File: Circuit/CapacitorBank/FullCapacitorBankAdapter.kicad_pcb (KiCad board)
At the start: 2 copper layers, 114.3 x 61 mm, 45 parts, among them J1 AC Power In, J2 Output+, J3 Output-, J4 To Control, T1 6:6:75+75, U1 L7812, U2 LM393, U3 LM393, U4 PC817

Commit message: [Circuit] Add a bypass diode to capacitor bank adapter for safety
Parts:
- added D7: 1N4007, Diode_THT:D_DO-41_SOD81_P10.16mm_Horizontal, F.Cu at (142.2, 64.8)
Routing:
- net /PowerOut-: track 107.3 -> 113.7 mm
- net /PowerOut+: track 96.8 -> 103.1 mm
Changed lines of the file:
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@@
     (thickness 1.6)
     (drawings 17)
-    (tracks 147)
+    (tracks 150)
     (zones 0)
-    (modules 45)
+    (modules 46)
     (nets 40)
   )
@@
     (add_net "Net-(R6-Pad2)")
     (add_net "Net-(R8-Pad2)")
+  )
+  (module Diode_THT:D_DO-41_SOD81_P10.16mm_Horizontal (layer F.Cu)
+    (at 142.24 64.77 270)
+    (descr "Diode, DO-41_SOD81 series, Axial, Horizontal, pin pitch=10.16mm, , length*diameter=5.2*2.7mm^2, , http://www.diodes.com/_files/packages/DO-41%20(Plastic).pdf")
+    (tags "Diode DO-41_SOD81 series Axial Horizontal pin pitch 10.16mm  length 5.2mm diameter 2.7mm")
+    (fp_text reference D7 (at 5.08 -2.47 90) (layer F.SilkS)
+      (effects (font (size 1 1) (thickness 0.15)))
+    )
+    (fp_text value 1N4007 (at 5.08 2.47 90) (layer F.Fab)
+      (effects (font (size 1 1) (thickness 0.15)))
+    )
+    (fp_text user K (at 0 -2.1 90) (layer F.SilkS)
+      (effects (font (size 1 1) (thickness 0.15)))
+    )
+    (fp_text user K (at 0 -2.1 90) (layer F.Fab)
+      (effects (font (size 1 1) (thickness 0.15)))
+    )
+    (fp_text user %R (at 5.47 0 90) (layer F.Fab)
+      (effects (font (size 1 1) (thickness 0.15)))
+    )
+    (fp_line (start 11.51 -1.6) (end -1.35 -1.6) (layer F.CrtYd) (width 0.05))
+    (fp_line (start 11.51 1.6) (end 11.51 -1.6) (layer F.CrtYd) (width 0.05))
+    (fp_line (start -1.35 1.6) (end 11.51 1.6) (layer F.CrtYd) (width 0.05))
+    (fp_line (start -1.35 -1.6) (end -1.35 1.6) (layer F.CrtYd) (width 0.05))
+    (fp_line (start 3.14 -1.47) (end 3.14 1.47) (layer F.SilkS) (width 0.12))
+    (fp_line (start 3.38 -1.47) (end 3.38 1.47) (layer F.SilkS) (width 0.12))
+    (fp_line (start 3.26 -1.47) (end 3.26 1.47) (layer F.SilkS) (width 0.12))
+    (fp_line (start 8.82 0) (end 7.8 0) (layer F.SilkS) (width 0.12))
+    (fp_line (start 1.34 0) (end 2.36 0) (layer F.SilkS) (width 0.12))
+    (fp_line (start 7.8 -1.47) (end 2.36 -1.47) (layer F.SilkS) (width 0.12))
+    (fp_line (start 7.8 1.47) (end 7.8 -1.47) (layer F.SilkS) (width 0.12))
+    (fp_line (start 2.36 1.47) (end 7.8 1.47) (layer F.SilkS) (width 0.12))
+    (fp_line (start 2.36 -1.47) (end 2.36 1.47) (layer F.SilkS) (width 0.12))
+    (fp_line (start 3.16 -1.35) (end 3.16 1.35) (layer F.Fab) (width 0.1))
+    (fp_line (start 3.36 -1.35) (end 3.36 1.35) (layer F.Fab) (width 0.1))
+    (fp_line (start 3.26 -1.35) (end 3.26 1.35) (layer F.Fab) (width 0.1))
+    (fp_line (start 10.16 0) (end 7.68 0) (layer F.Fab) (width 0.1))
+    (fp_line (start 0 0) (end 2.48 0) (layer F.Fab) (width 0.1))
+    (fp_line (start 7.68 -1.35) (end 2.48 -1.35) (layer F.Fab) (width 0.1))
+    (fp_line (start 7.68 1.35) (end 7.68 -1.35) (layer F.Fab) (width 0.1))
+    (fp_line (start 2.48 1.35) (end 7.68 1.35) (layer F.Fab) (width 0.1))
+    (fp_line (start 2.48 -1.35) (end 2.48 1.35) (layer F.Fab) (width 0.1))
+    (pad 2 thru_hole oval (at 10.16 0 270) (size 2.2 2.2) (drill 1.1) (layers *.Cu *.Mask)
+      (net 2 /PowerOut-))
+    (pad 1 thru_hole rect (at 0 0 270) (size 2.2 2.2) (drill 1.1) (layers *.Cu *.Mask)
+      (net 1 /PowerOut+))
+    (model ${KISYS3DMOD}/Diode_THT.3dshapes/D_DO-41_SOD81_P10.16mm_Horizontal.wrl
+      (at (xyz 0 0 0))
+      (scale (xyz 1 1 1))
+      (rotate (xyz 0 0 0))
+    )
   )
   (module Capacitor_THT:CP_Radial_D4.0mm_P2.00mm (layer F.Cu)
@@
   (gr_line (start 105.41 74.93) (end 115.57 74.93) (layer F.Mask) (width 0.15))
   (gr_circle (center 142.24 35.56) (end 143.51 35.56) (layer Edge.Cuts) (width 0.05))
-  (gr_text "M. Gong" (at 144.78 68.58) (layer F.SilkS)
+  (gr_text "M. Gong" (at 149.86 68.58) (layer F.SilkS)
     (effects (font (size 1 1) (thickness 0.15)))
   )
@@
   (segment (start 114.3 58.42) (end 106.68 58.42) (width 0.25) (layer B.Cu) (net 1))
   (segment (start 119.38 63.5) (end 124.46 58.42) (width 0.25) (layer B.Cu) (net 1) (status 10))
-  (segment (start 124.46 58.42) (end 148.59 58.42) (width 0.25) (layer B.Cu) (net 1))
+  (segment (start 142.24 64.77) (end 142.24 58.42) (width 0.25) (layer B.Cu) (net 1))
+  (segment (start 124.46 58.42) (end 142.24 58.42) (width 0.25) (layer B.Cu) (net 1))
+  (segment (start 142.24 58.42) (end 148.59 58.42) (width 0.25) (layer B.Cu) (net 1))
   (segment (start 88.98 76.12) (end 88.82 76.12) (width 0.25) (layer B.Cu) (net 2) (status 30))
   (segment (start 88.98 76.12) (end 88.98 81.28) (width 0.25) (layer B.Cu) (net 2) (status 30))
@@
   (segment (start 91.44 83.82) (end 88.98 81.36) (width 0.25) (layer B.Cu) (net 2) (status 20))
   (segment (start 88.9 81.28) (end 86.36 83.82) (width 0.25) (layer B.Cu) (net 2) (status 10))
+  (segment (start 142.24 74.93) (end 142.24 81.28) (width 0.25) (layer B.Cu) (net 2))
   (segment (start 114.3 71.12) (end 114.3 73.66) (width 0.25) (layer B.Cu) (net 3) (status 30))
   (segment (start 114.3 78.74) (end 114.3 76.2) (width 0.25) (layer B.Cu) (net 4) (status 30))

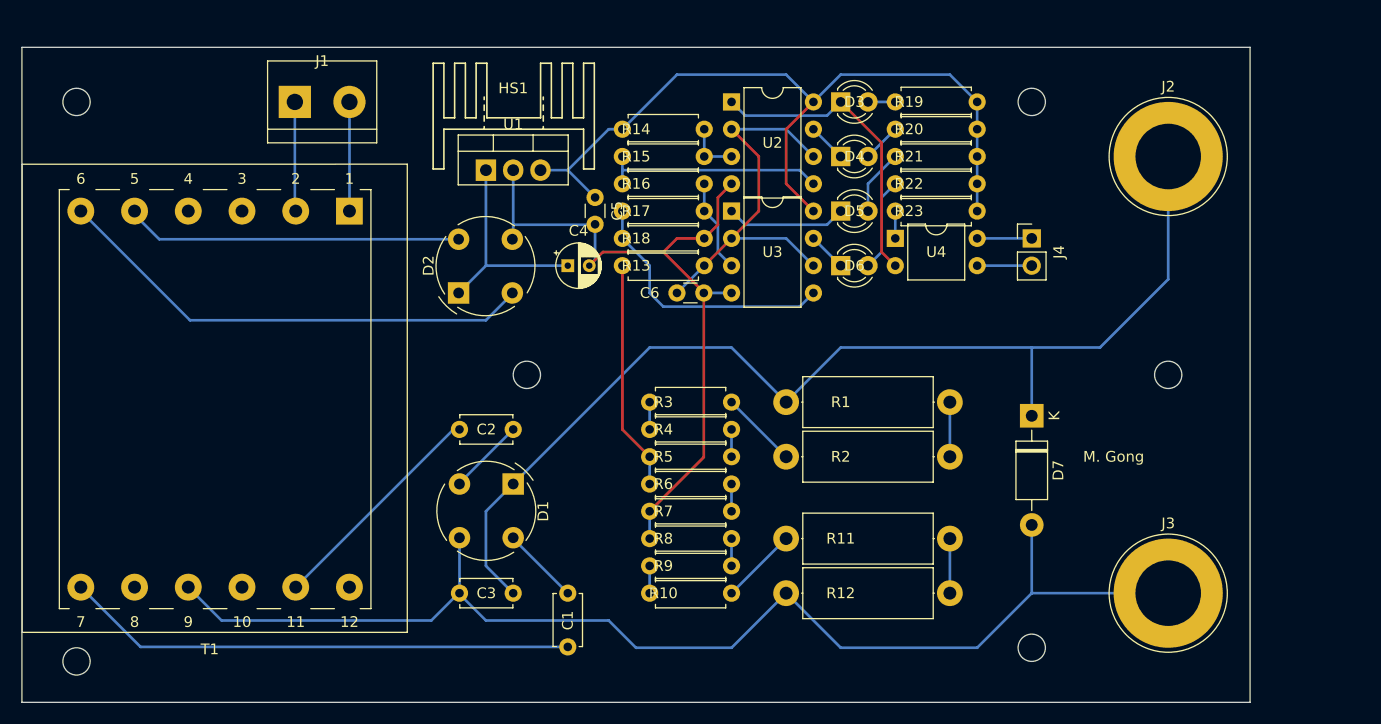
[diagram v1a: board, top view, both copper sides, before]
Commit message: [Circuit] Change the decoupling capacitors to a larger ones
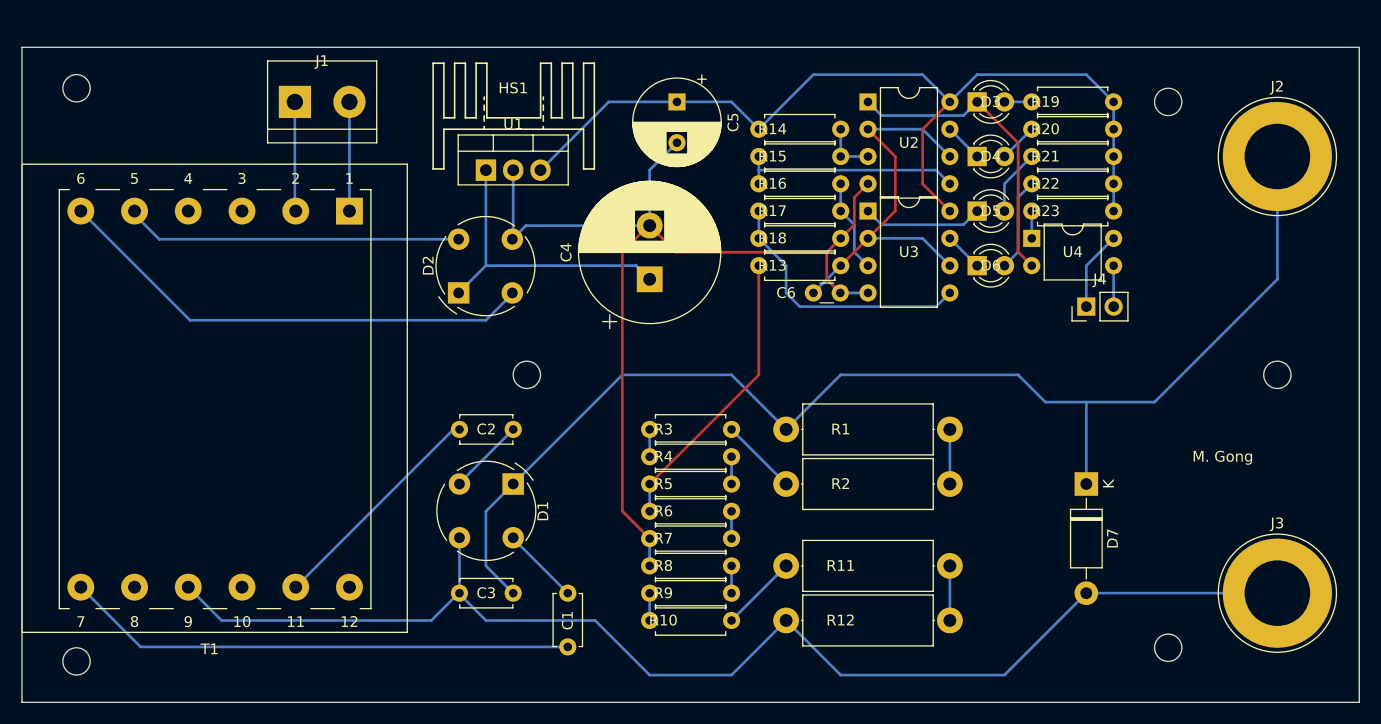
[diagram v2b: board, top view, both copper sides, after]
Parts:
- C4: value 1uF -> 2200uF; footprint Capacitor_THT:CP_Radial_D4.0mm_P2.00mm -> Capacitor_THT:CP_Radial_D13.0mm_P5.00mm
- C5: footprint Capacitor_THT:C_Disc_D3.0mm_W1.6mm_P2.50mm -> Capacitor_THT:CP_Radial_D8.0mm_P3.80mm
- moved R19 12.7 mm to (149.9, 35.6)
- moved R20 12.7 mm to (149.9, 38.1)
- moved R21 12.7 mm to (149.9, 40.6)
- moved R22 12.7 mm to (149.9, 43.2)
- moved R23 12.7 mm to (142.2, 45.7)
- moved U4 12.7 mm to (142.2, 48.3)
- moved C6 12.7 mm to (121.9, 53.3)
- moved D3 12.7 mm to (137.2, 35.6)
- moved D4 12.7 mm to (137.2, 40.6)
- moved D5 12.7 mm to (137.2, 45.7)
- moved D6 12.7 mm to (137.2, 50.8)
- moved R15 12.7 mm to (116.8, 40.6)
- moved R17 12.7 mm to (116.8, 45.7)
- moved U2 12.7 mm to (127.0, 35.6)
- moved U3 12.7 mm to (127.0, 45.7)
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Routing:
- net GND: track 69.1 -> 94.9 mm
- net /PowerOut+: track 103.1 -> 116.6 mm
- net +12V: track 73.5 -> 84.7 mm
- net Net-(C4-Pad1): track 20.1 -> 28.2 mm
- net /PowerOut-: track 113.7 -> 119.6 mm
- net Net-(R13-Pad2): track 21.4 -> 27.1 mm
- net /ControlSignal: track 5.08 -> 7.40 mm
- net /ControlGND: track 5.08 -> 3.81 mm
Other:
- board size 114.3 x 61 mm -> 124.5 x 61 mm

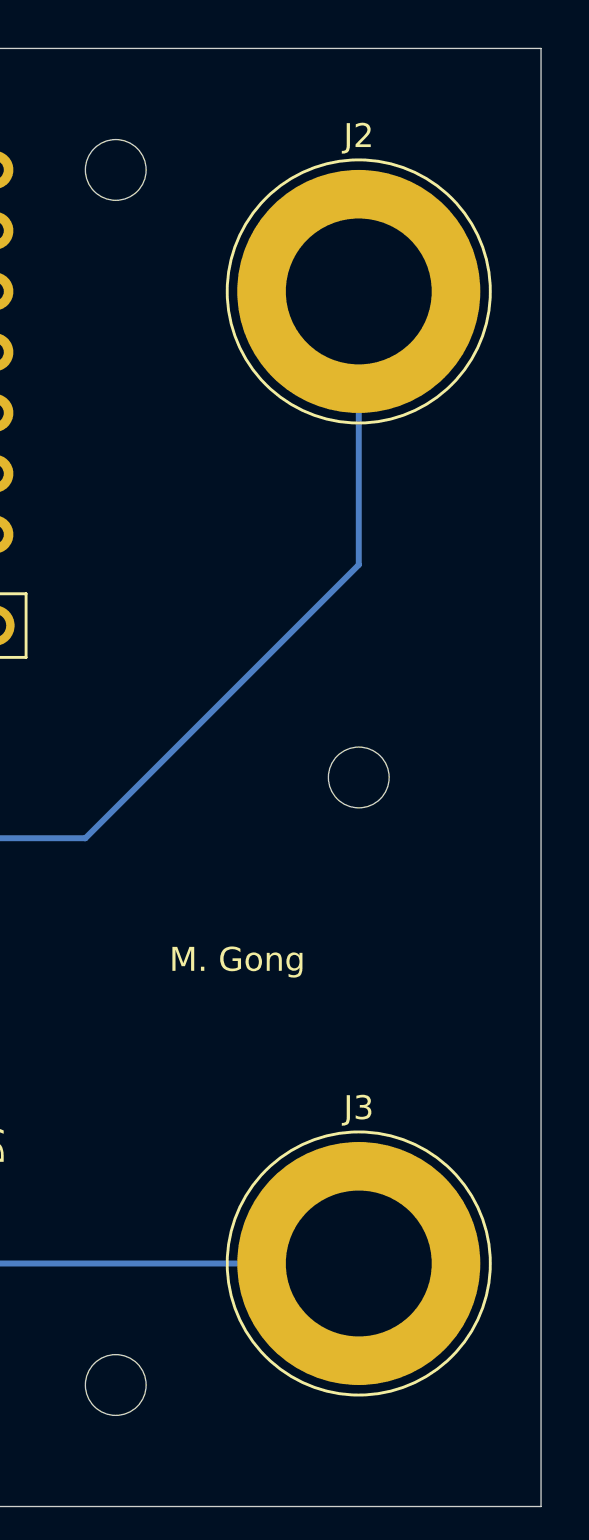
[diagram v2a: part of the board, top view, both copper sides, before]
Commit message: [Circuit] Use M6 bolt as the connectors of capacitor bank and starter
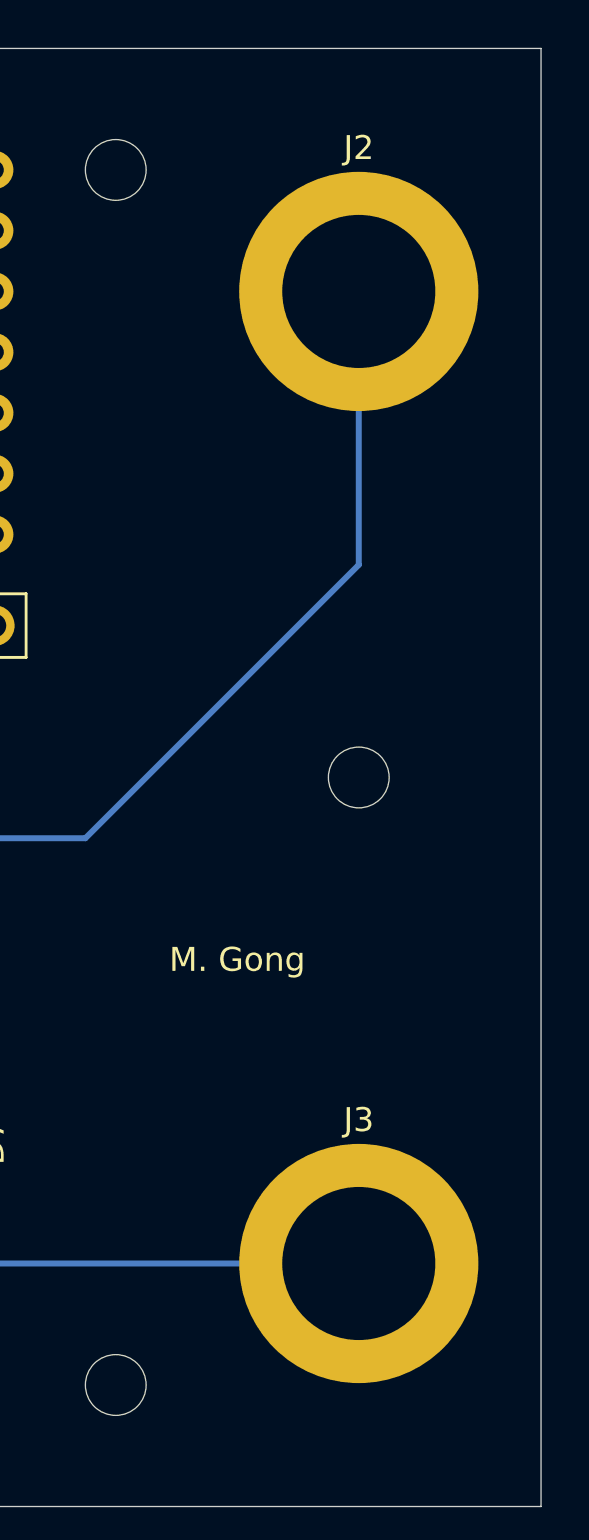
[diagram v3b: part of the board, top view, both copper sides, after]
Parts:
- J2, J3: footprint Connector:Banana_Jack_1Pin -> MountingHole:MountingHole_6.4mm_M6_ISO14580_Pad
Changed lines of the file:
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@@
     (add_net "Net-(R8-Pad2)")
+  )
+  (module MountingHole:MountingHole_6.4mm_M6_ISO14580_Pad (layer F.Cu)
+    (at 165.1 40.64)
+    (descr "Mounting Hole 6.4mm, M6, ISO14580")
+    (tags "mounting hole 6.4mm m6 iso14580")
+    (attr virtual)
+    (fp_text reference J2 (at 0 -6) (layer F.SilkS)
+      (effects (font (size 1 1) (thickness 0.15)))
+    )
+    (fp_text value Output+ (at 0 6) (layer F.Fab)
+      (effects (font (size 1 1) (thickness 0.15)))
+    )
+    (fp_circle (center 0 0) (end 5.25 0) (layer F.CrtYd) (width 0.05))
+    (fp_circle (center 0 0) (end 5 0) (layer Cmts.User) (width 0.15))
+    (fp_text user %R (at 0.3 0) (layer F.Fab)
+      (effects (font (size 1 1) (thickness 0.15)))
+    )
+    (pad 1 thru_hole circle (at 0 0) (size 10 10) (drill 6.4) (layers *.Cu *.Mask)
+      (net 1 /PowerOut+))
+  )
+  (module MountingHole:MountingHole_6.4mm_M6_ISO14580_Pad (layer F.Cu)
+    (at 165.1 81.28)
+    (descr "Mounting Hole 6.4mm, M6, ISO14580")
+    (tags "mounting hole 6.4mm m6 iso14580")
+    (attr virtual)
+    (fp_text reference J3 (at 0 -6) (layer F.SilkS)
+      (effects (font (size 1 1) (thickness 0.15)))
+    )
+    (fp_text value Output- (at 0 6) (layer F.Fab)
+      (effects (font (size 1 1) (thickness 0.15)))
+    )
+    (fp_circle (center 0 0) (end 5.25 0) (layer F.CrtYd) (width 0.05))
+    (fp_circle (center 0 0) (end 5 0) (layer Cmts.User) (width 0.15))
+    (fp_text user %R (at 0.3 0) (layer F.Fab)
+      (effects (font (size 1 1) (thickness 0.15)))
+    )
+    (pad 1 thru_hole circle (at 0 0) (size 10 10) (drill 6.4) (layers *.Cu *.Mask)
+      (net 2 /PowerOut-))
   )
   (module Capacitor_THT:CP_Radial_D13.0mm_P5.00mm (layer F.Cu)
@@
     )
   )
-  (module Connector:Banana_Jack_1Pin (layer F.Cu)
-    (at 165.1 81.28)
-    (descr "Single banana socket, footprint - 6mm drill")
-    (tags "banana socket")
-    (fp_text reference J3 (at 0 -6.5) (layer F.SilkS)
-      (effects (font (size 1 1) (thickness 0.15)))
-    )
-    (fp_text value Output- (at -0.25 6.5) (layer F.Fab)
-      (effects (font (size 1 1) (thickness 0.15)))
-    )
-    (fp_circle (center 0 0) (end 5.5 0) (layer F.SilkS) (width 0.12))
-    (fp_circle (center 0 0) (end 4.85 0.05) (layer F.Fab) (width 0.1))
-    (fp_circle (center 0 0) (end 2 0) (layer F.Fab) (width 0.1))
-    (fp_circle (center 0 0) (end 5.75 0) (layer F.CrtYd) (width 0.05))
-    (fp_text user %R (at 0 0) (layer F.Fab)
-      (effects (font (size 0.8 0.8) (thickness 0.12)))
-    )
-    (pad 1 thru_hole circle (at 0 0) (size 10.16 10.16) (drill 6.1) (layers *.Cu *.Mask)
-      (net 2 /PowerOut-))
-    (model ${KISYS3DMOD}/Connector.3dshapes/Banana_Jack_1Pin.wrl
-      (at (xyz 0 0 0))
-      (scale (xyz 2 2 2))
-      (rotate (xyz 0 0 0))
-    )
-  )
   (module Resistor_THT:R_Axial_DIN0414_L11.9mm_D4.5mm_P15.24mm_Horizontal (layer F.Cu)
     (at 119.38 66.04)
@@
       (rotate (xyz 0 0 0))
     )
-  )
-  (module Connector:Banana_Jack_1Pin (layer F.Cu)
-    (at 165.1 40.64)
-    (descr "Single banana socket, footprint - 6mm drill")
-    (tags "banana socket")
-    (fp_text reference J2 (at 0 -6.5) (layer F.SilkS)
-      (effects (font (size 1 1) (thickness 0.15)))
-    )
-    (fp_text value Output+ (at -0.25 6.5) (layer F.Fab)
-      (effects (font (size 1 1) (thickness 0.15)))
-    )
-    (fp_text user %R (at 0 0) (layer F.Fab)
-      (effects (font (size 0.8 0.8) (thickness 0.12)))
-    )
-    (fp_circle (center 0 0) (end 5.75 0) (layer F.CrtYd) (width 0.05))
-    (fp_circle (center 0 0) (end 2 0) (layer F.Fab) (width 0.1))
-    (fp_circle (center 0 0) (end 4.85 0.05) (layer F.Fab) (width 0.1))
-    (fp_circle (center 0 0) (end 5.5 0) (layer F.SilkS) (width 0.12))
-    (pad 1 thru_hole circle (at 0 0) (size 10.16 10.16) (drill 6.1) (layers *.Cu *.Mask)
-      (net 1 /PowerOut+))
-    (model ${KISYS3DMOD}/Connector.3dshapes/Banana_Jack_1Pin.wrl
-      (at (xyz 0 0 0))
-      (scale (xyz 2 2 2))
-      (rotate (xyz 0 0 0))
-    )
